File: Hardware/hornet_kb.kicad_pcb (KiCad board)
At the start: 4 copper layers, 199.5 x 120.1 mm, 155 parts, among them J1 Conn_ST_STDC14, J10 USB_C_Receptacle_USB2.0, J2 Conn_01x03, SW1 ESC, SW10 TAB, SW11 Q, SW12 W, SW13 E, SW14 R, SW15 T, SW17 M1, SW18 CAPS, SW19 A, SW2 `, SW20 S, SW21 D, SW22 F, SW23 G, SW25 M2, SW26 M3, SW27 SW_DPDT_x2, SW28 SHIFT, SW29 CTRL, SW3 1, SW30 Rot_Enc, SW31 Z, SW32 WIN, SW34 X, SW35 FN, SW37 C, SW38 ALT, SW4 2, SW40 V, SW41 SPACE, SW43 B, SW44 DEL, SW5 3, SW6 4, SW7 5, SW8 6, SW9 M0, SW98 SW_Push, U1 nRF52840, U2 BQ24040, U3 BQ51050BRHL, U4 AP22814BW5, U5 TPS2116DRL, Y1 32.768kHz, Y3 Crystal_GND24

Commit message: ADded cardinal
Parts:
- L1: footprint Connector_JST:JST_EH_S2B-EH_1x02_P2.50mm_Horizontal -> TerminalBlock_Phoenix:TerminalBlock_Phoenix_MKDS-1,5-2-5.08_1x02_P5.08mm_Horizontal
- moved JP4 3.45 mm to (225.5, 78.2)
- moved L1 3.08 mm to (223.4, 65.3)
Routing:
- net Net-(U3-AC2): track 56.4 -> 59.7 mm
- net Net-(C13-Pad1): track 42.7 -> 39.5 mm
- net Net-(JP1-A): track 16.8 -> 19.9 mm
- net +BATT: track 110.8 -> 112.2 mm
- net /R_COL_6: track 148.7 -> 150.0 mm
- net Net-(JP3-A): track 52.3 -> 51.7 mm
- added copper zone on In2.Cu, net VDD
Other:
- board text added: "Aryan Ghosh Rev1 Hornet Keyboard LEFTHAND"

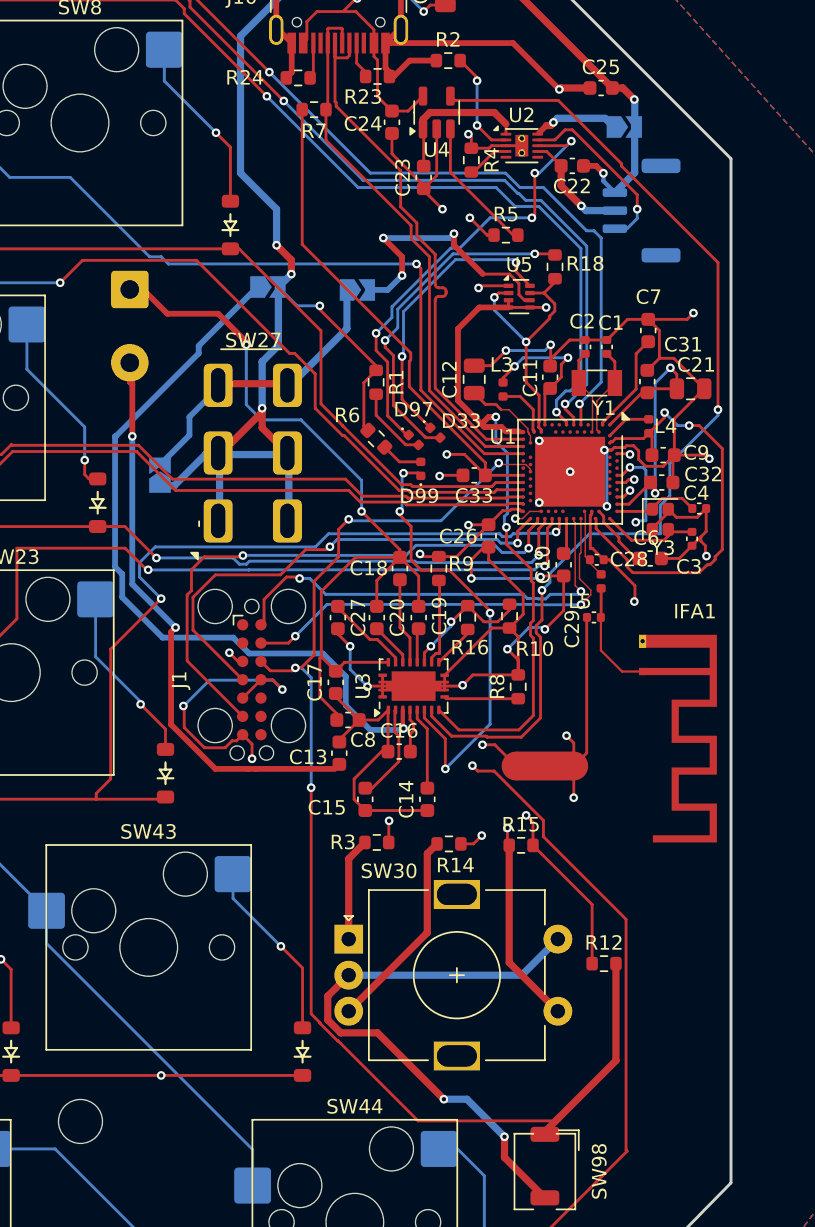
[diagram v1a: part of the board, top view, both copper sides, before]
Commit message: Add LCSC part numbers and new resistor to PCB
Added LCSC part numbers to multiple components in hornet_kb.kicad_pcb for improved BOM generation. Introduced a new 500Ω resistor (R11) and updated net assignments for Q1 and D27. Modified .gitignore to exclude backup and auto-save files, and removed obsolete backup files from Hardware/hornet_kb-backups. Made symbol and footprint tweaks in Custom_sym.kicad_sym.
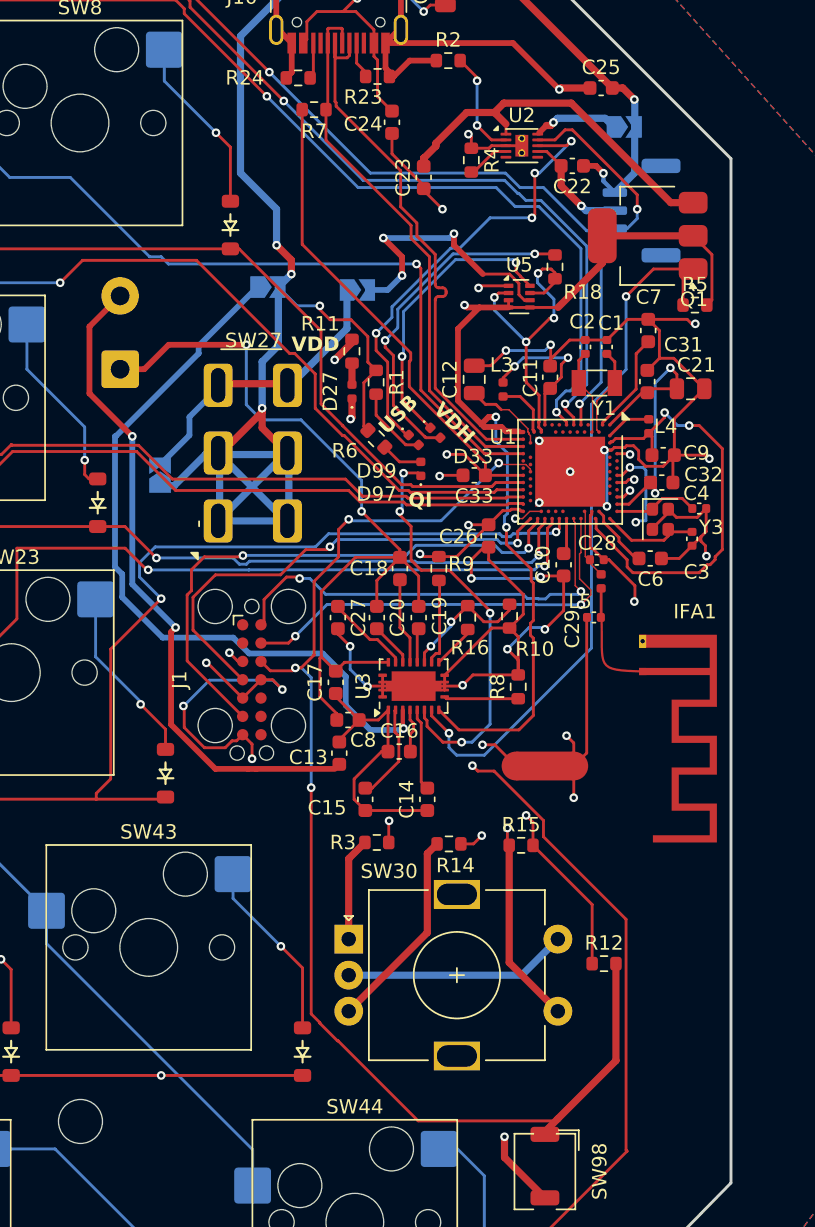
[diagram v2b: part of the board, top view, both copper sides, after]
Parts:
- removed U4: AP22814BW5, Package_TO_SOT_SMD:SOT-23-5
- added D27: VDD, LED_SMD:LED_0402_1005Metric, F.Cu at (238.8, 72.4)
- added Q1: BTS4140N, Package_TO_SOT_SMD:SOT-223, F.Cu at (259.3, 61.6)
- added R11: 500, Resistor_SMD:R_0603_1608Metric, F.Cu at (238.8, 69.6)
- Y3: value Crystal_GND24 -> 32Mhz
- moved R5 14.0 mm to (262.6, 66.4)
- moved L1 5.57 mm to (222.8, 70.9), turned to 90 degrees
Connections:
- R5 pad 1: VBUS -> Net-(Q1-IN)
- R5 pad 2: Net-(U4-~{FLG}) -> VBUS
- U3 pad 8: Net-(U3-~{AD-EN}) -> Net-(Q1-IN)
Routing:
- net Net-(U3-~{AD-EN}): track 72.3 -> 0.00 mm, vias 2 -> 0
- net Net-(Q1-IN): track 0.00 -> 49.9 mm, vias 0 -> 2
- net +BATT: track 112.2 -> 131.3 mm
- net GND: track 251.8 -> 233.0 mm, vias 29 -> 30
- net Net-(Q1-OUT): track 10.2 -> 25.6 mm
- net VBUS: track 74.5 -> 89.7 mm, vias 6 -> 5
- net Net-(U4-~{FLG}): track 9.49 -> 0.00 mm
- net Net-(C13-Pad1): track 39.5 -> 45.8 mm
- net Net-(IFA1-ANT): track 7.81 -> 2.00 mm
- net VDDH: track 18.4 -> 21.9 mm, vias 2 -> 4
- net Net-(D99-K): track 31.6 -> 29.1 mm
- net VDD: track 93.0 -> 94.9 mm, vias 11 -> 12
- net Net-(D27-A): track 0.00 -> 1.49 mm
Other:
- board text added: "BATT_ENA"
- board text added: "QI"
- board text added: "QI_ENA"
- board text added: "SKIP_SW"
- board text added: "USB"
- board text added: "USB_CHG_ENA"
- board text added: "VDD"
- board text added: "VDH"

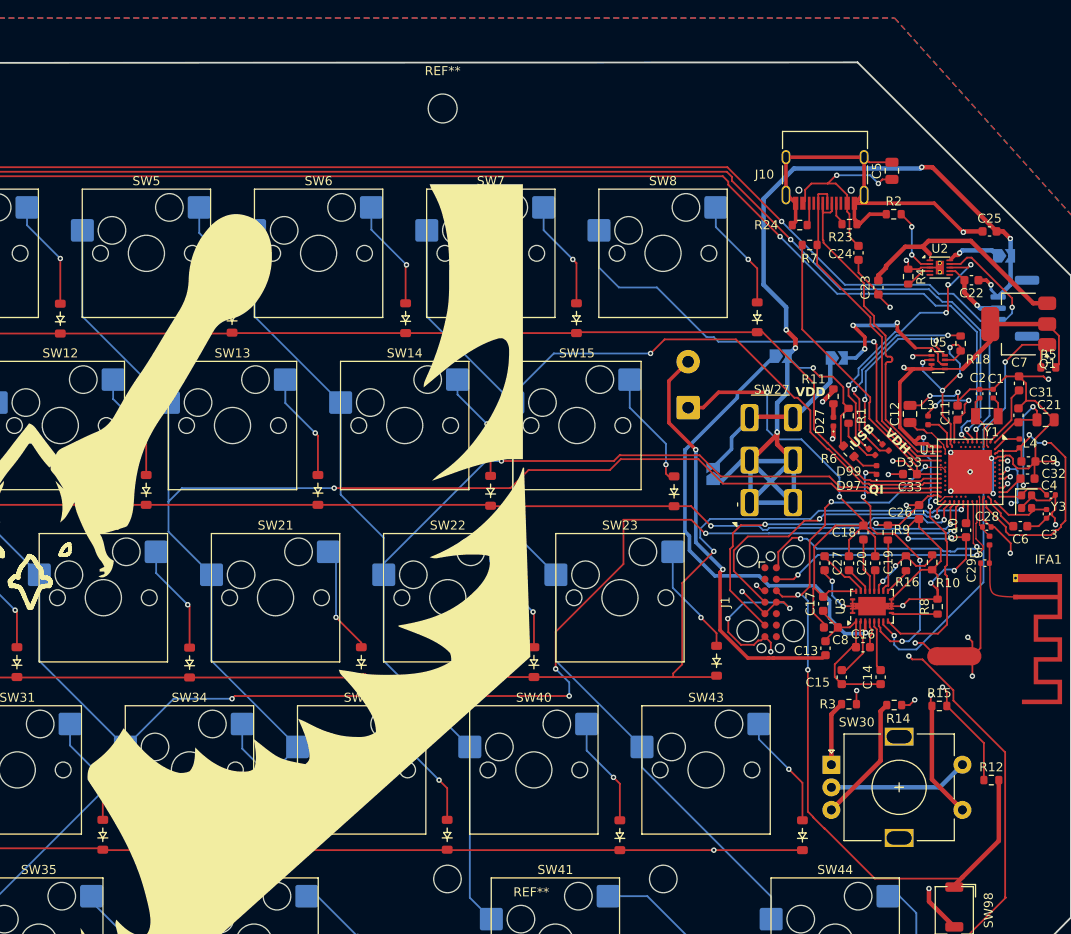
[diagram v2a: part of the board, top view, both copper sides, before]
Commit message: Added LCSC part defs
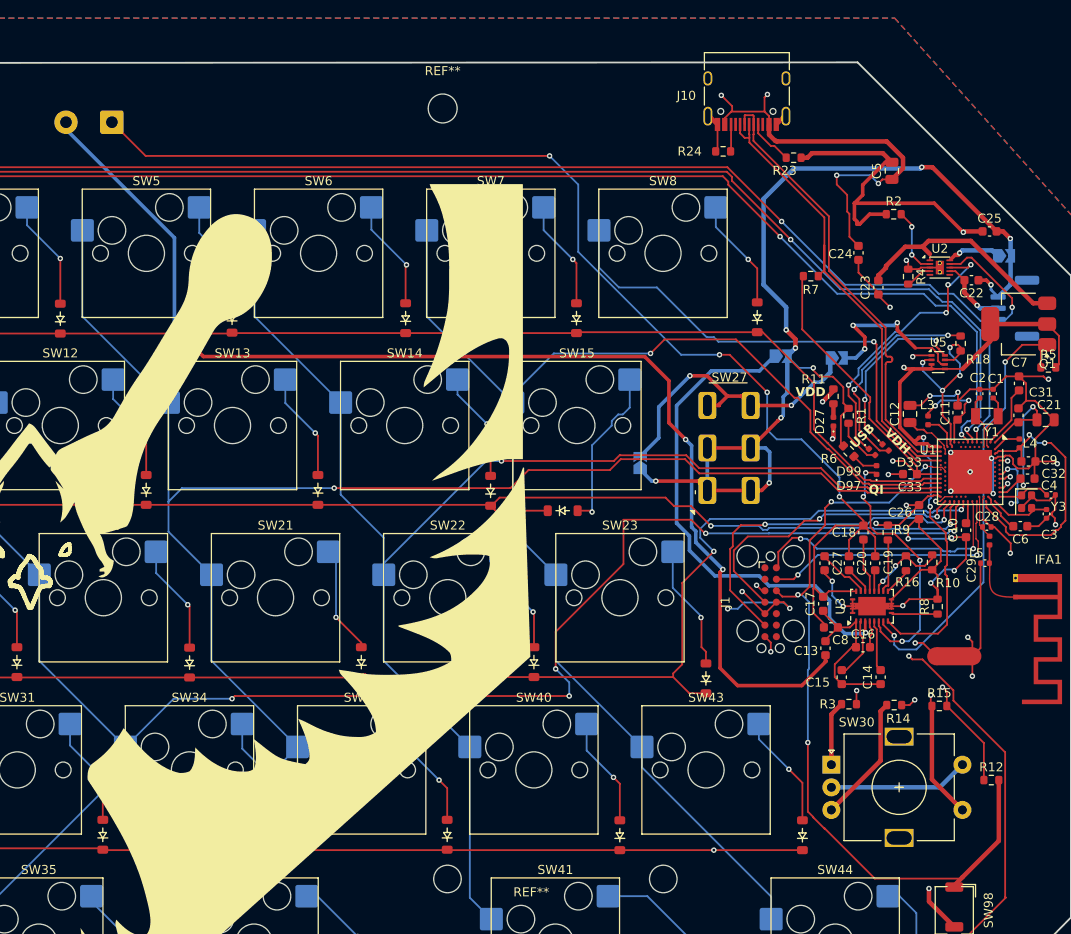
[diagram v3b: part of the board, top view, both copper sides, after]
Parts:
- moved L1 71.1 mm to (159.0, 39.3), turned to 180 degrees
- moved D15 12.5 mm to (208.9, 82.3), turned to 0 degrees
- moved J10 12.3 mm to (229.3, 35.5)
- moved R24 11.8 mm to (226.6, 42.5)
- moved R23 9.60 mm to (234.4, 43.2)
- moved JP4 8.16 mm to (217.5, 77.0)
- moved SW27 4.86 mm to (224.9, 80.0)
- moved R7 3.45 mm to (236.3, 56.3)
- moved D23 2.27 mm to (224.7, 100.8)
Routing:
- net Net-(C13-Pad1): track 45.8 -> 132.8 mm, vias 2 -> 3
- net Net-(U3-AC2): track 59.4 -> 139.2 mm, vias 2 -> 4
- net VBUS: track 89.7 -> 115.2 mm, vias 5 -> 7
- net /D+: track 38.0 -> 52.9 mm
- net Net-(JP1-A): track 19.9 -> 33.9 mm, vias 0 -> 2
- net +BATT: track 131.3 -> 119.2 mm, vias 7 -> 9
- net /D-: track 38.3 -> 50.3 mm
- net GND: track 233.0 -> 223.3 mm
- net /R_ROW_1: track 158.8 -> 166.2 mm
- net Net-(D15-A): track 13.1 -> 18.3 mm
- net Net-(JP3-A): track 51.7 -> 55.5 mm
- net VDD: track 94.9 -> 91.3 mm
- net Net-(J10-CC1): track 2.27 -> 5.19 mm
- net Net-(D23-A): track 12.4 -> 13.9 mm
- net /R_ROW_3: track 214.6 -> 215.5 mm
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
